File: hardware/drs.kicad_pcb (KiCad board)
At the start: 2 copper layers, 60 x 40 mm, 4 parts

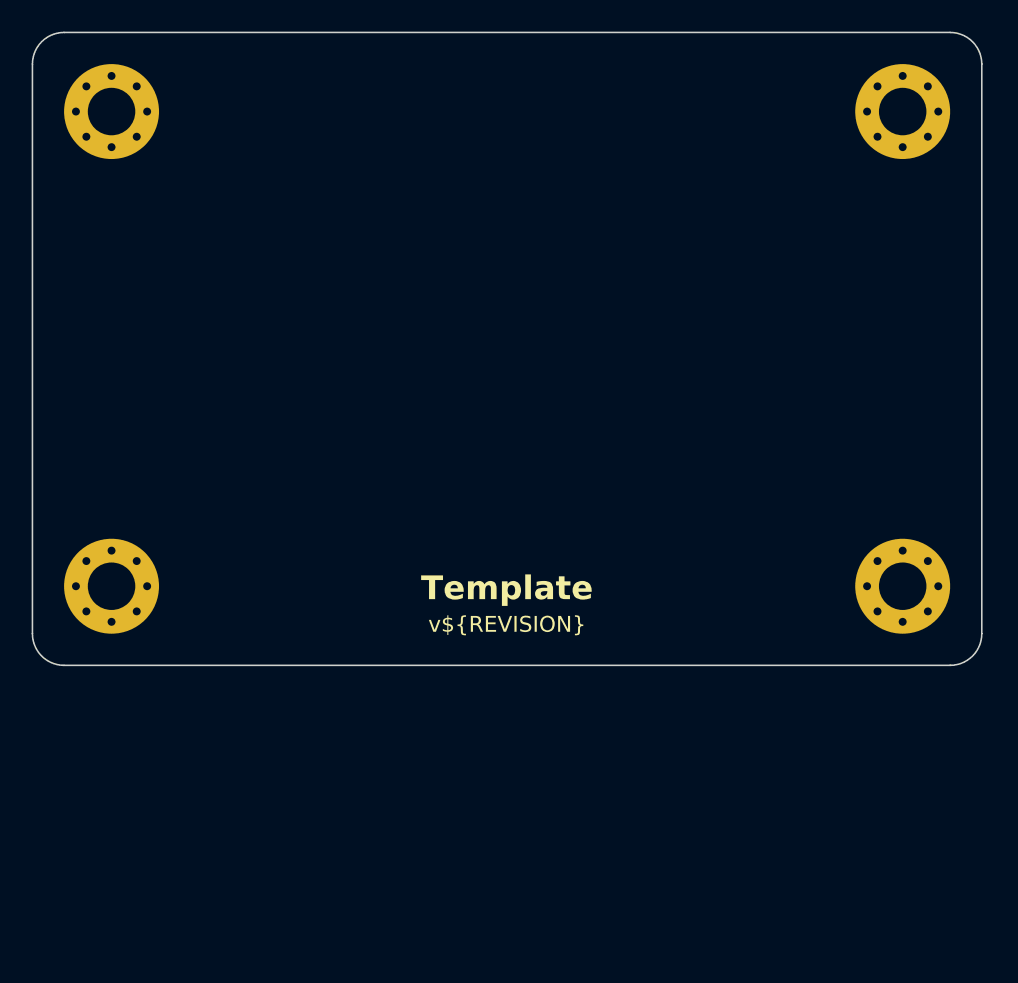
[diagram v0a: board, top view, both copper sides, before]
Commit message: pcb scheme update - general/basic aligment
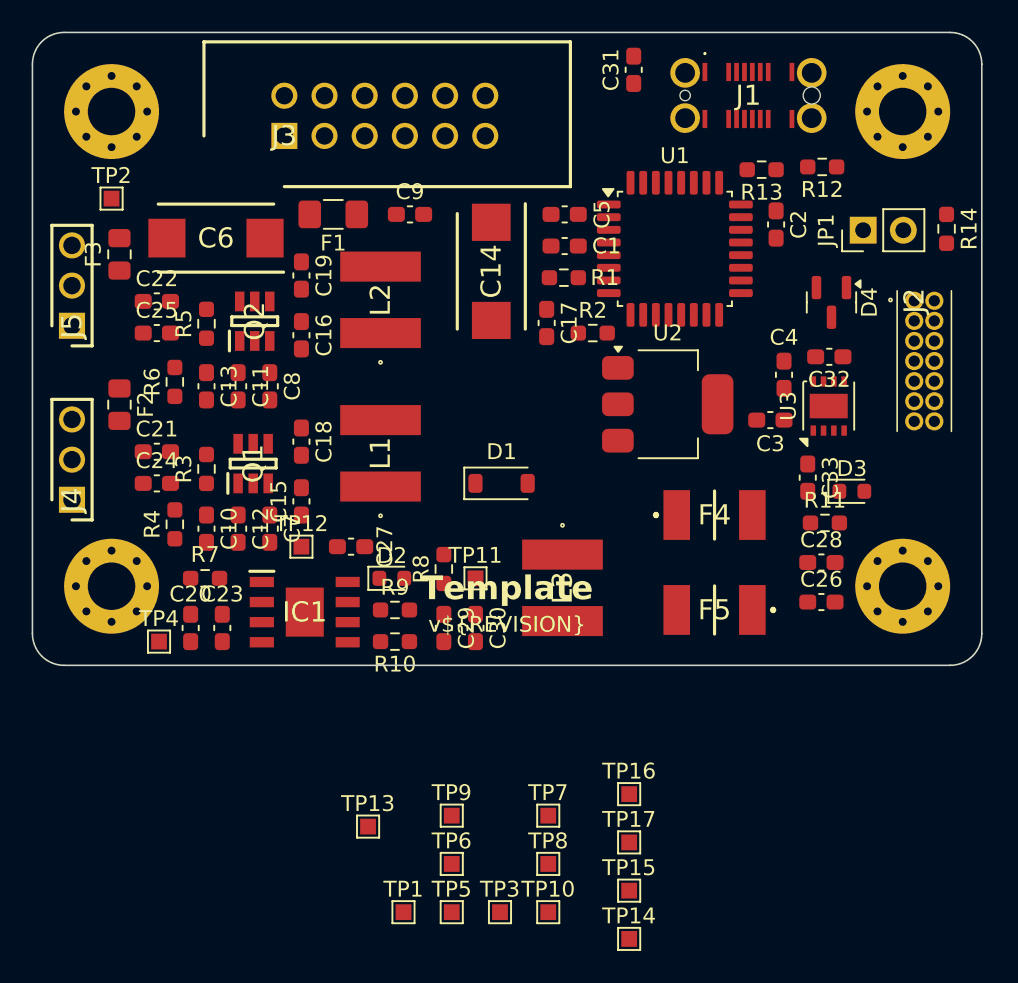
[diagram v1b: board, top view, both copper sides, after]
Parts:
- added C1: 10u, Capacitor_SMD:C_0603_1608Metric_Pad1.08x0.95mm_HandSolder, F.Cu at (149.6, 89.5)
- added C10: 1u, Capacitor_SMD:C_0603_1608Metric_Pad1.08x0.95mm_HandSolder, F.Cu at (127.0, 107.4)
- added C11: 1u, Capacitor_SMD:C_0603_1608Metric_Pad1.08x0.95mm_HandSolder, F.Cu at (129.0, 98.4)
- added C12: 1u, Capacitor_SMD:C_0603_1608Metric_Pad1.08x0.95mm_HandSolder, F.Cu at (129.0, 107.4)
- added C13: 1u, Capacitor_SMD:C_0603_1608Metric_Pad1.08x0.95mm_HandSolder, F.Cu at (127.0, 98.4)
- added C14: 22u, SamacSys_Parts:CAPPM7343X310N, F.Cu at (145.0, 91.1)
- added C15: 100n, Capacitor_SMD:C_0603_1608Metric_Pad1.08x0.95mm_HandSolder, F.Cu at (133.0, 105.6)
- added C16: 100n, Capacitor_SMD:C_0603_1608Metric_Pad1.08x0.95mm_HandSolder, F.Cu at (133.0, 95.1)
- added C17: 10u, Capacitor_SMD:C_0603_1608Metric_Pad1.08x0.95mm_HandSolder, F.Cu at (148.5, 94.4)
- added C18: 100n, Capacitor_SMD:C_0603_1608Metric_Pad1.08x0.95mm_HandSolder, F.Cu at (133.0, 101.9)
- added C19: 100n, Capacitor_SMD:C_0603_1608Metric_Pad1.08x0.95mm_HandSolder, F.Cu at (133.0, 91.4)
- added C2: 100n, Capacitor_SMD:C_0603_1608Metric_Pad1.08x0.95mm_HandSolder, F.Cu at (163.0, 88.1)
- added C20: 10u, Capacitor_SMD:C_0603_1608Metric_Pad1.08x0.95mm_HandSolder, F.Cu at (126.0, 113.6)
- added C21: 47u, Capacitor_SMD:C_0603_1608Metric_Pad1.08x0.95mm_HandSolder, F.Cu at (123.9, 102.5)
- added C22: 47u, Capacitor_SMD:C_0603_1608Metric_Pad1.08x0.95mm_HandSolder, F.Cu at (123.9, 93.0)
- added C23: 100n, Capacitor_SMD:C_0603_1608Metric_Pad1.08x0.95mm_HandSolder, F.Cu at (128.0, 113.6)
- added C24: 47u, Capacitor_SMD:C_0603_1608Metric_Pad1.08x0.95mm_HandSolder, F.Cu at (123.9, 104.5)
- added C25: 47u, Capacitor_SMD:C_0603_1608Metric_Pad1.08x0.95mm_HandSolder, F.Cu at (123.9, 95.0)
- added C26: 100n, Capacitor_SMD:C_0603_1608Metric_Pad1.08x0.95mm_HandSolder, F.Cu at (165.9, 112.0)
- added C27: 100n, Capacitor_SMD:C_0603_1608Metric_Pad1.08x0.95mm_HandSolder, F.Cu at (136.1, 108.5)
- added C28: 100n, Capacitor_SMD:C_0603_1608Metric_Pad1.08x0.95mm_HandSolder, F.Cu at (165.9, 109.5)
- added C29: 47u, Capacitor_SMD:C_0603_1608Metric_Pad1.08x0.95mm_HandSolder, F.Cu at (142.0, 113.6)
- added C3: 4u7, Capacitor_SMD:C_0603_1608Metric_Pad1.08x0.95mm_HandSolder, F.Cu at (162.6, 100.5)
- added C30: 47u, Capacitor_SMD:C_0603_1608Metric_Pad1.08x0.95mm_HandSolder, F.Cu at (144.0, 113.6)
- added C31: 10n, Capacitor_SMD:C_0603_1608Metric_Pad1.08x0.95mm_HandSolder, F.Cu at (154.0, 78.4)
- added C32: 100n, Capacitor_SMD:C_0603_1608Metric_Pad1.08x0.95mm_HandSolder, F.Cu at (166.4, 96.5)
- added C33: 100n, Capacitor_SMD:C_0603_1608Metric_Pad1.08x0.95mm_HandSolder, F.Cu at (165.0, 104.1)
- added C4: 100n, Capacitor_SMD:C_0603_1608Metric_Pad1.08x0.95mm_HandSolder, F.Cu at (163.5, 97.6)
- added C5: 4u7, Capacitor_SMD:C_0603_1608Metric_Pad1.08x0.95mm_HandSolder, F.Cu at (149.6, 87.5)
- added C6: 22u, SamacSys_Parts:CAPPM7343X310N, F.Cu at (127.6, 89.0)
- added C7: 1u, Capacitor_SMD:C_0603_1608Metric_Pad1.08x0.95mm_HandSolder, F.Cu at (131.0, 107.4)
- added C8: 1u, Capacitor_SMD:C_0603_1608Metric_Pad1.08x0.95mm_HandSolder, F.Cu at (131.0, 98.4)
- added C9: 10u, Capacitor_SMD:C_0603_1608Metric_Pad1.08x0.95mm_HandSolder, F.Cu at (139.9, 87.5)
- added D1: D_Schottky_Small, Diode_SMD:D_SOD-123, F.Cu at (145.7, 104.5)
- added D2: +5V, LED_SMD:LED_0603_1608Metric, F.Cu at (138.7, 110.5)
- added D3: +3V3, LED_SMD:LED_0603_1608Metric, F.Cu at (167.8, 105.0)
- added D4: PESD2CAN.215, Package_TO_SOT_SMD:SOT-23, F.Cu at (166.5, 93.1)
- added F1: Polyfuse_Small, Fuse:Fuse_1206_3216Metric_Pad1.42x1.75mm_HandSolder, F.Cu at (135.0, 87.5)
- added F2: Polyfuse_Small, Fuse:Fuse_0805_2012Metric_Pad1.15x1.40mm_HandSolder, F.Cu at (121.5, 99.5)
- added F3: Polyfuse_Small, Fuse:Fuse_0805_2012Metric_Pad1.15x1.40mm_HandSolder, F.Cu at (121.5, 90.0)
- added F4: Polyfuse_Small, SamacSys_Parts:MINIASMDC260F162, F.Cu at (159.1, 106.5)
- added F5: Polyfuse_Small, SamacSys_Parts:MINIASMDC260F162, F.Cu at (159.1, 112.5)
- added IC1: LMR38020FDDAR, SamacSys_Parts:SOIC127P600X170-9N, F.Cu at (133.2, 112.6)
- added J1: USB_C_Receptacle_USB2.0_16P, SamacSys_Parts:USB4145030230C, F.Cu at (161.2, 80.0)
- added J2: FTSH-107-01-L-D-K, SamacSys_Parts:FTSH-107-XX-YYY-D-K, F.Cu at (171.7, 93.0)
- added J3: POWER & CAN & SPI2, SamacSys_Parts:SHDR12W64P254X254_2X6_2286X895X915P, F.Cu at (131.9, 82.5)
- added J4: PWM1, SamacSys_Parts:HDRV3W64P0X254_1X3_762X254X864P, F.Cu at (118.5, 105.5)
- added J5: PWM2, SamacSys_Parts:HDRV3W64P0X254_1X3_762X254X864P, F.Cu at (118.5, 94.5)
- added JP1: Jumper_2_Bridged, Connector_PinHeader_2.54mm:PinHeader_1x02_P2.54mm_Vertical, F.Cu at (168.5, 88.5)
- added L1: 12u/3A, SamacSys_Parts:VLS6045, F.Cu at (138.0, 102.6)
- added L2: 12u/3A, SamacSys_Parts:VLS6045, F.Cu at (138.0, 92.9)
- added L3: 15u/2A, SamacSys_Parts:VLS6045, F.Cu at (149.5, 111.1)
- added Q1: LMR51635XDDCR, SamacSys_Parts:SOT95P280X110-6N, F.Cu at (129.9, 103.2)
- added Q2: LMR51635XDDCR, SamacSys_Parts:SOT95P280X110-6N, F.Cu at (130.1, 94.2)
- added R1: 0, Resistor_SMD:R_0603_1608Metric_Pad0.98x0.95mm_HandSolder, F.Cu at (149.6, 91.5)
- added R10: 10k, Resistor_SMD:R_0603_1608Metric_Pad0.98x0.95mm_HandSolder, F.Cu at (138.9, 114.5)
- added R11: 1k, Resistor_SMD:R_0603_1608Metric_Pad0.98x0.95mm_HandSolder, F.Cu at (166.1, 107.0)
- added R12: 5k1, Resistor_SMD:R_0603_1608Metric_Pad0.98x0.95mm_HandSolder, F.Cu at (165.9, 84.5)
- added R13: 5k1, Resistor_SMD:R_0603_1608Metric_Pad0.98x0.95mm_HandSolder, F.Cu at (162.1, 84.7)
- added R14: 120R, Resistor_SMD:R_0603_1608Metric_Pad0.98x0.95mm_HandSolder, F.Cu at (173.8, 88.4)
- added R2: 100k, Resistor_SMD:R_0603_1608Metric_Pad0.98x0.95mm_HandSolder, F.Cu at (151.4, 95.0)
- added R3: 100k, Resistor_SMD:R_0603_1608Metric_Pad0.98x0.95mm_HandSolder, F.Cu at (127.0, 103.6)
- added R4: 13k7, Resistor_SMD:R_0603_1608Metric_Pad0.98x0.95mm_HandSolder, F.Cu at (125.0, 107.1)
- added R5: 100k, Resistor_SMD:R_0603_1608Metric_Pad0.98x0.95mm_HandSolder, F.Cu at (127.0, 94.4)
- added R6: 13k7, Resistor_SMD:R_0603_1608Metric_Pad0.98x0.95mm_HandSolder, F.Cu at (125.0, 98.1)
- added R7: 64k9, Resistor_SMD:R_0603_1608Metric_Pad0.98x0.95mm_HandSolder, F.Cu at (126.9, 110.5)
- added R8: 1k, Resistor_SMD:R_0603_1608Metric_Pad0.98x0.95mm_HandSolder, F.Cu at (142.0, 109.9)
- added R9: 40k2, Resistor_SMD:R_0603_1608Metric_Pad0.98x0.95mm_HandSolder, F.Cu at (138.9, 112.5)
- added TP1: TP_VCC, TestPoint:TestPoint_Pad_1.0x1.0mm, F.Cu at (139.4, 131.6)
- added TP10: TP_+3V3, TestPoint:TestPoint_Pad_1.0x1.0mm, F.Cu at (148.6, 131.6)
- added TP11: TP_+5V, TestPoint:TestPoint_Pad_1.0x1.0mm, F.Cu at (144.0, 110.5)
- added TP12: TP_+5V, TestPoint:TestPoint_Pad_1.0x1.0mm, F.Cu at (133.0, 108.5)
- added TP13: TP_VBUS, TestPoint:TestPoint_Pad_1.0x1.0mm, F.Cu at (137.2, 126.2)
- added TP14: TP_+3V3, TestPoint:TestPoint_Pad_1.0x1.0mm, F.Cu at (153.7, 133.3)
- added TP15: TP_+5V, TestPoint:TestPoint_Pad_1.0x1.0mm, F.Cu at (153.7, 130.2)
- added TP16: TP_CAN_H, TestPoint:TestPoint_Pad_1.0x1.0mm, F.Cu at (153.7, 124.1)
- added TP17: TP_CAN_L, TestPoint:TestPoint_Pad_1.0x1.0mm, F.Cu at (153.7, 127.2)
- added TP2: TP_VCC, TestPoint:TestPoint_Pad_1.0x1.0mm, F.Cu at (121.0, 86.5)
- added TP3: TP_VCC, TestPoint:TestPoint_Pad_1.0x1.0mm, F.Cu at (145.6, 131.6)
- added TP4: TP_VCC, TestPoint:TestPoint_Pad_1.0x1.0mm, F.Cu at (124.0, 114.5)
- added TP5: TP_+6V6S1, TestPoint:TestPoint_Pad_1.0x1.0mm, F.Cu at (142.5, 131.6)
- added TP6: TP_+6V6S1, TestPoint:TestPoint_Pad_1.0x1.0mm, F.Cu at (142.5, 128.6)
- added TP7: TP_+6V6S2, TestPoint:TestPoint_Pad_1.0x1.0mm, F.Cu at (148.6, 125.5)
- added TP8: TP_+6V6S2, TestPoint:TestPoint_Pad_1.0x1.0mm, F.Cu at (148.6, 128.6)
- added TP9: TP_+5V, TestPoint:TestPoint_Pad_1.0x1.0mm, F.Cu at (142.5, 125.5)
- added U1: STM32G0C1KCTxN, Package_QFP:LQFP-32_7x7mm_P0.8mm, F.Cu at (156.6, 89.7)
- added U2: LM1117-3.3, Package_TO_SOT_SMD:SOT-223-3_TabPin2, F.Cu at (156.2, 99.5)
- added U3: MCP2542FDxMF, Package_DFN_QFN:DFN-8-1EP_3x3mm_P0.65mm_EP1.55x2.4mm, F.Cu at (166.3, 99.6)

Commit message: Items assebled
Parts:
- removed C31: 10n, Capacitor_SMD:C_0603_1608Metric_Pad1.08x0.95mm_HandSolder
- J1: value USB_C_Receptacle_USB2.0_16P -> USB-C_GCT_USB4145-03-0070-C
- TP9: value TP_+5V -> T_+5V
- moved T10 51.3 mm to (172.2, 86.1), turned to 180 degrees
- moved T5 49.0 mm to (129.8, 84.2)
- moved T3 43.9 mm to (147.5, 87.8)
- moved TP9 39.4 mm to (166.8, 94.5)
- moved T1 39.2 mm to (142.2, 92.5)
- moved T14 35.8 mm to (154.8, 97.5)
- moved J1 32.3 mm to (161.5, 112.2)
- moved T13 30.6 mm to (161.5, 107.5)
- moved T17 29.9 mm to (157.0, 97.5)
- moved T15 28.3 mm to (166.5, 105.0)
- moved T7 27.5 mm to (126.8, 108.8)
- moved T16 25.1 mm to (162.8, 100.8)
- moved C2 24.8 mm to (141.7, 100.8), turned to 180 degrees
- moved C10 24.5 mm to (142.5, 88.4)
- moved C12 24.2 mm to (144.0, 88.4)
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- renumbered TP1 to T1, TP10 to T10, TP11 to T11, TP12 to T12, TP13 to T13, TP14 to T14, TP15 to T15, TP16 to T16, TP17 to T17, TP2 to T2, TP3 to T3, TP4 to T4, TP5 to T5, TP6 to T6, TP7 to T7, TP8 to T8
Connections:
- C14 pad 1: VCC -> /Power/VCC_IN
- C17 pad 1: VCC -> /Power/VCC_IN
- C21 pad 2: +6V6S1 -> /Power/+6V6S1_OUT
- C22 pad 2: +6V6S2 -> /Power/+6V6S2_OUT
- C24 pad 2: +6V6S1 -> /Power/+6V6S1_OUT
- C25 pad 2: +6V6S2 -> /Power/+6V6S2_OUT
- C6 pad 1: VCC -> /Power/VCC_IN
- C9 pad 1: VCC -> /Power/VCC_IN
- F1 pad 2: VCC -> /Power/VCC_IN
- F2 pad 2: +6V6S1 -> /Power/+6V6S1_OUT
- F3 pad 2: +6V6S2 -> /Power/+6V6S2_OUT
- J1 pad A6: /Connectors/D+ -> /Connectors/D-
- J1 pad B7: /Connectors/D- -> /Connectors/D+
- J2 pad 4: /Connectors/DIO -> /Connectors/CLK
- J2 pad 6: /Connectors/CLK -> /Connectors/DIO
- J3 pad 6: CAN_H -> unconnected-(J3-Pin_6-Pad6)
- L1 pad 2: +6V6S1 -> /Power/+6V6S1_OUT
- L2 pad 2: +6V6S2 -> /Power/+6V6S2_OUT
- R3 pad 2: +6V6S1 -> /Power/+6V6S1_OUT
- R5 pad 2: +6V6S2 -> /Power/+6V6S2_OUT
- T1 pad 1: VCC -> /Power/VCC_IN
- T5 pad 1: +6V6S1 -> /Power/+6V6S1_OUT
- T7 pad 1: +6V6S2 -> /Power/+6V6S2_OUT
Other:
- board text removed: "Template"
- board text removed: "v${REVISION}"
